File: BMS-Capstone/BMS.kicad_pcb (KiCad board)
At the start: 4 copper layers, 235 x 92.7 mm, 164 parts, among them IC1 MP2643, IC2 MP2643, IC3 MP2643, IC4 MP2643, IC5 MP2643, IC6 MP2643, IC7 BQ7694204PFBR, J1 Conn_01x02_Socket, J2 Conn_01x02_Socket, J3 Conn_01x13_Socket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

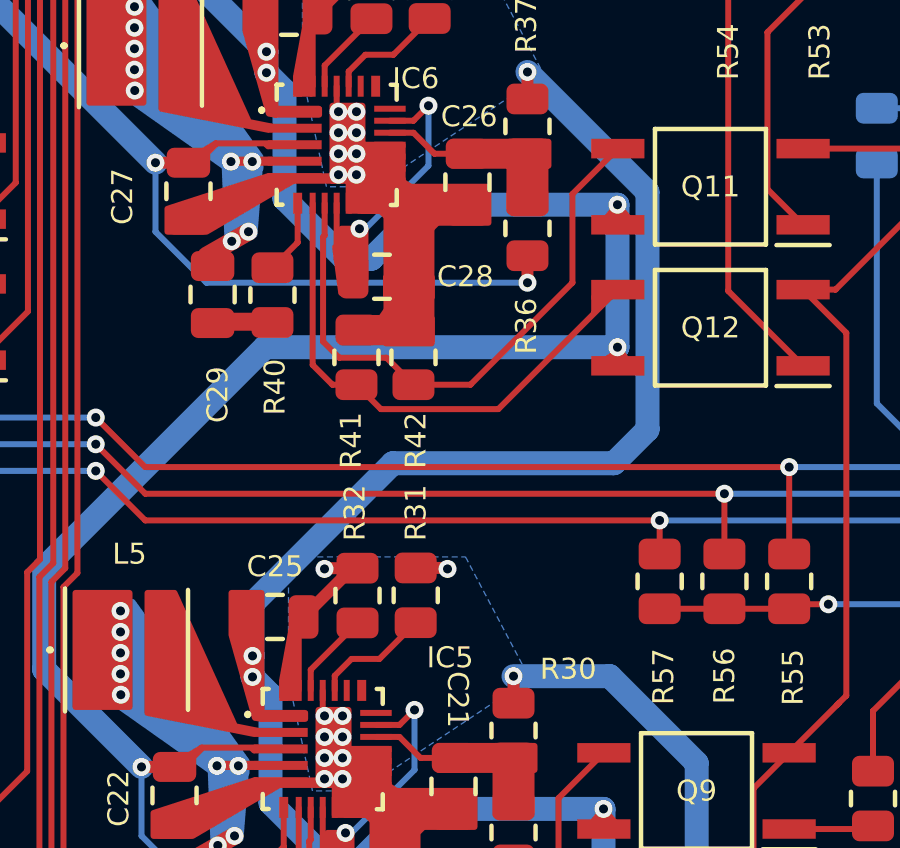
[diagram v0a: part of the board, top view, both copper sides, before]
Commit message: Added V-CUT label
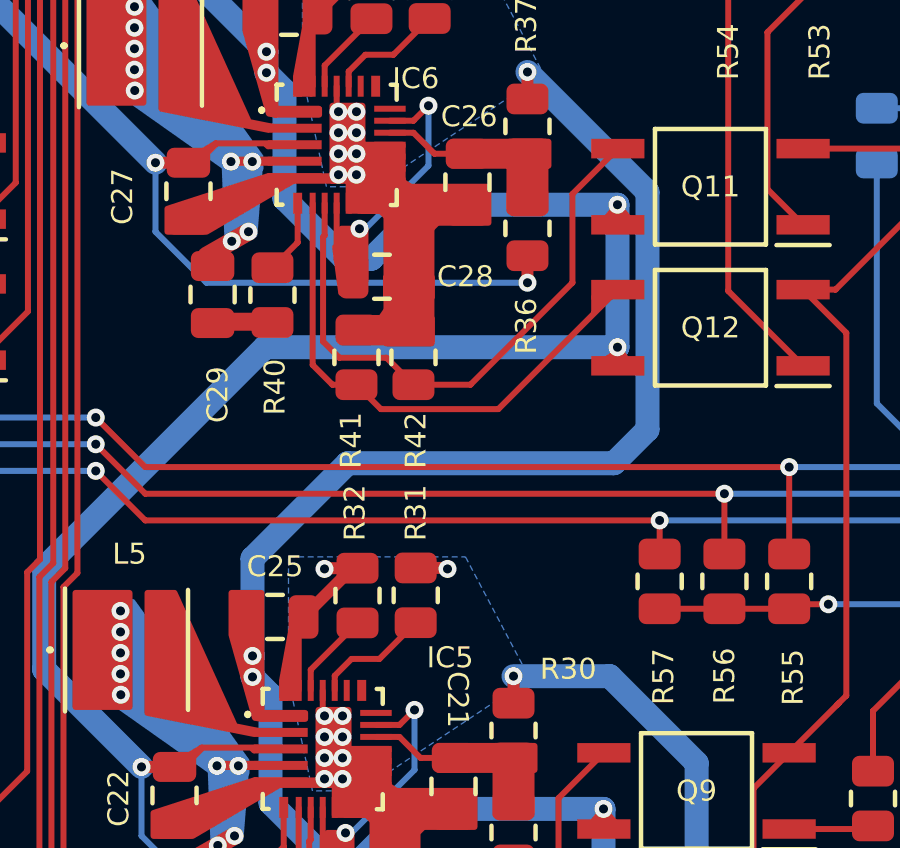
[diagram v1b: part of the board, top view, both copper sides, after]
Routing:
- net /BMS Board/4Upper: track 311.4 -> 312.2 mm
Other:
- board text added: "V-CUT"

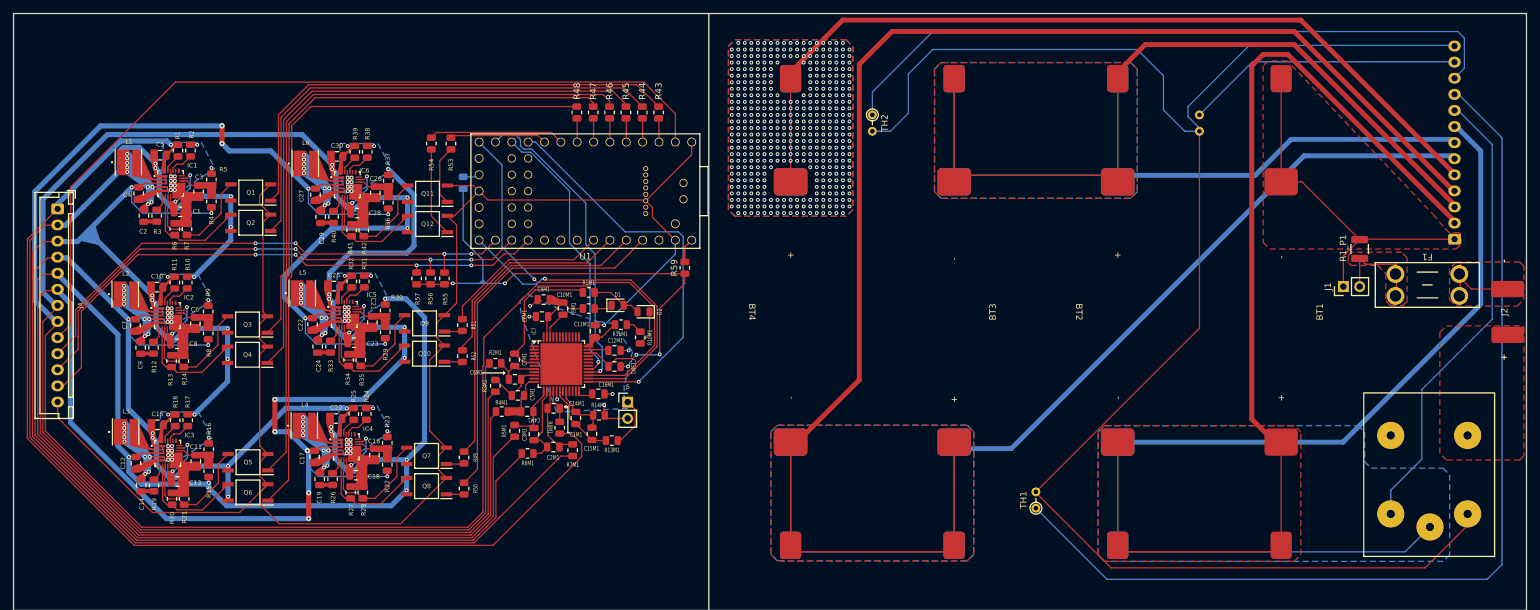
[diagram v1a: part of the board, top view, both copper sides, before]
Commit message: Added Transistors for optocouple and relay drive
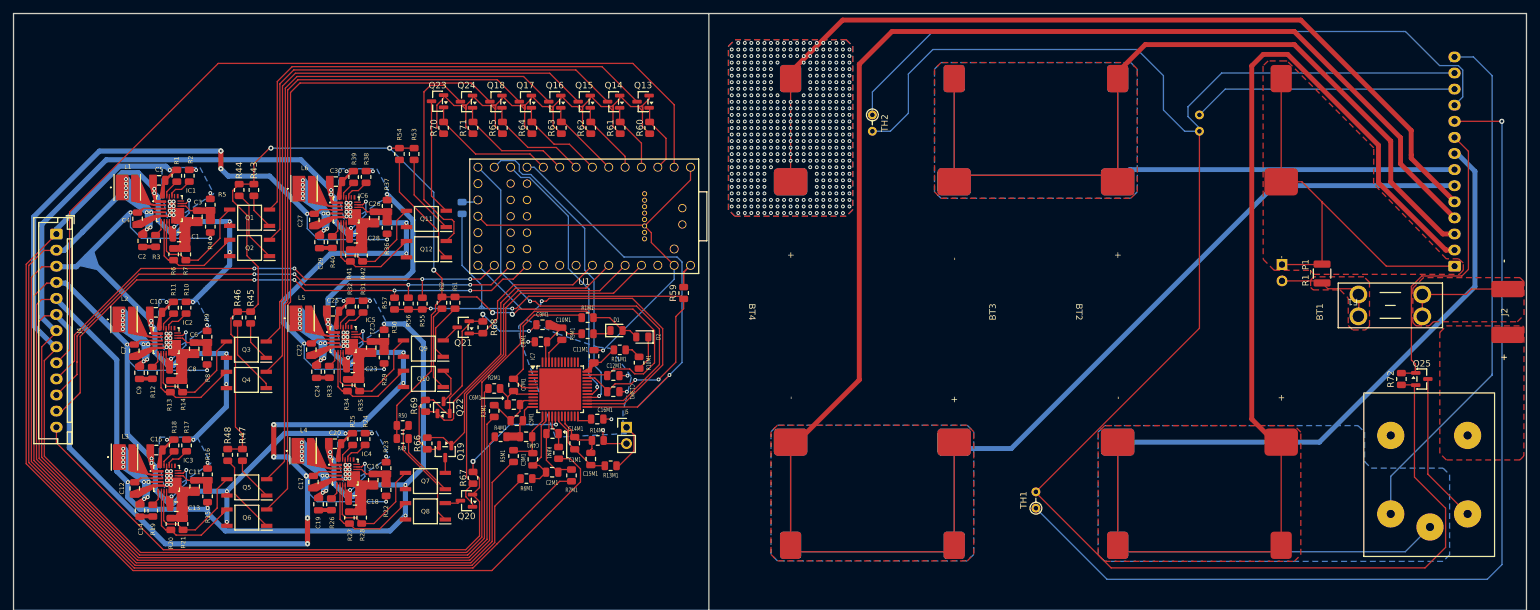
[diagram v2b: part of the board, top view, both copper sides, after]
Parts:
- added Q13: 2N7002, Package_TO_SOT_SMD:SOT-23, F.Cu at (124.3, 43.0)
- added Q14: 2N7002, Package_TO_SOT_SMD:SOT-23, F.Cu at (119.7, 43.0)
- added Q15: 2N7002, Package_TO_SOT_SMD:SOT-23, F.Cu at (115.1, 43.0)
- added Q16: 2N7002, Package_TO_SOT_SMD:SOT-23, F.Cu at (110.6, 43.0)
- added Q17: 2N7002, Package_TO_SOT_SMD:SOT-23, F.Cu at (106.0, 43.0)
- added Q18: 2N7002, Package_TO_SOT_SMD:SOT-23, F.Cu at (101.4, 43.0)
- added Q19: 2N7002, Package_TO_SOT_SMD:SOT-23, F.Cu at (93.5, 97.4)
- added Q20: 2N7002, Package_TO_SOT_SMD:SOT-23, F.Cu at (96.8, 105.0)
- added Q21: 2N7002, Package_TO_SOT_SMD:SOT-23, F.Cu at (96.3, 78.1)
- added Q22: 2N7002, Package_TO_SOT_SMD:SOT-23, F.Cu at (93.3, 90.5)
- added Q23: 2N7002, Package_TO_SOT_SMD:SOT-23, F.Cu at (92.4, 43.0)
- added Q24: 2N7002, Package_TO_SOT_SMD:SOT-23, F.Cu at (96.8, 43.0)
- added Q25: 2N7002, Package_TO_SOT_SMD:SOT-23, F.Cu at (245.2, 86.1)
- added R60: 10k, Resistor_SMD:R_0805_2012Metric, F.Cu at (125.3, 47.1)
- added R61: 10k, Resistor_SMD:R_0805_2012Metric, F.Cu at (120.7, 47.1)
- added R62: 10k, Resistor_SMD:R_0805_2012Metric, F.Cu at (116.2, 47.1)
- added R63: 10k, Resistor_SMD:R_0805_2012Metric, F.Cu at (111.6, 47.1)
- added R64: 10k, Resistor_SMD:R_0805_2012Metric, F.Cu at (107.0, 47.1)
- added R65: 10k, Resistor_SMD:R_0805_2012Metric, F.Cu at (102.4, 47.1)
- added R66: 10k, Resistor_SMD:R_0805_2012Metric, F.Cu at (90.8, 96.1)
- added R67: 10k, Resistor_SMD:R_0805_2012Metric, F.Cu at (97.9, 101.4)
- added R68: 10k, Resistor_SMD:R_0805_2012Metric, F.Cu at (99.4, 78.1)
- added R69: 10k, Resistor_SMD:R_0805_2012Metric, F.Cu at (90.5, 90.3)
- added R70: 10k, Resistor_SMD:R_0805_2012Metric, F.Cu at (93.3, 47.1)
- added R71: 10k, Resistor_SMD:R_0805_2012Metric, F.Cu at (97.9, 47.1)
- added R72: 10k, Resistor_SMD:R_0805_2012Metric, F.Cu at (242.1, 86.1)
- J1: moved to B.Cu
- J3: value Conn_01x13_Socket -> Conn_01x14_Socket; footprint Connector_JST:JST_XH_S13B-XH-A-1_1x13_P2.50mm_Horizontal -> Connector_JST:JST_XH_S14B-XH-A-1_1x14_P2.50mm_Horizontal
- R43, R44, R45, R46, R47, R48, R49, R50, R51, R52, R53, R54: value 200 -> 720
- moved R47 76.1 mm to (62.1, 97.9), turned to 90 degrees
- moved R48 76.0 mm to (59.8, 97.9), turned to 90 degrees
- moved R45 66.4 mm to (63.3, 76.6), turned to 90 degrees
- moved R46 66.0 mm to (61.3, 76.6), turned to 90 degrees
- moved R43 64.0 mm to (63.8, 56.7), turned to 90 degrees
- moved R44 63.8 mm to (61.5, 56.7), turned to 90 degrees
- moved R50 13.7 mm to (86.9, 93.3), turned to 180 degrees
- moved J1 10.1 mm to (223.5, 68.3), turned to 180 degrees
- moved R49 9.97 mm to (86.9, 95.4), turned to 180 degrees
- moved R52 8.87 mm to (93.0, 74.3)
- moved R1_P1 6.97 mm to (229.7, 69.7)
- moved F1 6.58 mm to (235.4, 73.0)
- moved R53 5.94 mm to (88.7, 51.2)
- moved R54 5.22 mm to (86.4, 51.2)
- moved R56 5.20 mm to (87.8, 74.4)
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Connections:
- C12M1 pad 1: /Monitoring/5V -> /BMS Board/5v
- IC7 pad 35: /Monitoring/5V -> /BMS Board/5v
- K1 pad 2: MCUGND -> Net-(Q25-D)
- K1 pad 6: Net-(J3-Pin_9) -> Net-(J3-Pin_14)
- Q1 pad 2: GND -> Net-(Q13-D)
- Q10 pad 2: GND -> Net-(Q22-D)
- Q11 pad 2: GND -> Net-(Q23-D)
- Q12 pad 2: GND -> Net-(Q24-D)
- Q2 pad 2: GND -> Net-(Q14-D)
- Q3 pad 2: GND -> Net-(Q15-D)
- Q4 pad 2: GND -> Net-(Q16-D)
- Q5 pad 2: GND -> Net-(Q17-D)
- Q6 pad 2: GND -> Net-(Q18-D)
- Q7 pad 2: GND -> Net-(Q19-D)
- Q8 pad 2: GND -> Net-(Q20-D)
- Q9 pad 2: GND -> Net-(Q21-D)
- R43 pad 2: /BMS Board/1MODE -> /BMS Board/5v
- R44 pad 2: /BMS Board/1EN -> /BMS Board/5v
- R45 pad 2: /BMS Board/2MODE -> /BMS Board/5v
- R46 pad 2: /BMS Board/2EN -> /BMS Board/5v
- R47 pad 2: /BMS Board/3MODE -> /BMS Board/5v
- R48 pad 2: /BMS Board/3EN -> /BMS Board/5v
- R49 pad 2: /BMS Board/4MODE -> /BMS Board/5v
- R50 pad 2: /BMS Board/4EN -> /BMS Board/5v
- R51 pad 2: /BMS Board/5MODE -> /BMS Board/5v
- R52 pad 2: /BMS Board/5EN -> /BMS Board/5v
- R53 pad 2: /BMS Board/6MODE -> /BMS Board/5v
- R54 pad 2: /BMS Board/6EN -> /BMS Board/5v
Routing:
- net /BMS Board/5v: track 0.00 -> 184.5 mm, vias 0 -> 5
- net Net-(Q17-D): track 0.00 -> 99.8 mm
- net Net-(Q18-D): track 0.00 -> 99.1 mm
- net Net-(Q5-Pad1): track 105.0 -> 6.96 mm
- net Net-(Q6-Pad1): track 105.5 -> 12.6 mm
- net Net-(Q15-D): track 0.00 -> 89.3 mm
- net Net-(Q16-D): track 0.00 -> 88.6 mm
- net Net-(Q3-Pad1): track 90.3 -> 6.36 mm
- net Net-(J3-Pin_14): track 0.00 -> 82.7 mm
- net Net-(Q4-Pad1): track 91.9 -> 11.9 mm
- net Net-(Q13-D): track 0.00 -> 79.5 mm
- net Net-(Q14-D): track 0.00 -> 78.7 mm
- net Net-(Q1-Pad1): track 76.2 -> 5.67 mm
- net Net-(Q2-Pad1): track 77.5 -> 11.4 mm
- net GND: track 267.9 -> 309.2 mm, vias 8 -> 10
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- added copper zone on F.Cu, net GND

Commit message: Fixed up edge cuts and other DRC
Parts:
- moved C12 6.20 mm to (44.1, 97.0)
- moved C16 6.20 mm to (81.2, 95.7)
- moved C17 6.20 mm to (71.9, 96.0)
- moved C19 6.20 mm to (72.7, 99.5)
- moved C1M1 6.20 mm to (109.0, 88.5)
- moved C20 6.20 mm to (75.2, 90.1)
- moved C21 6.20 mm to (80.8, 75.2)
- moved C22 6.20 mm to (71.5, 75.5)
- moved C25 6.20 mm to (74.9, 69.5)
- moved C4 6.20 mm to (44.5, 55.1)
- moved C6M1 6.20 mm to (103.0, 84.0)
- moved C7 6.20 mm to (44.0, 75.6)
- moved IC4 6.20 mm to (76.8, 94.5)
- moved IC5 6.20 mm to (76.5, 73.9)
- moved L5 6.20 mm to (69.9, 70.6)
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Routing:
- net GND: track 309.2 -> 310.7 mm, vias 10 -> 11
- net /BMS Board/1GND: track 174.1 -> 174.8 mm
- net /BMS Board/5v: track 184.5 -> 185.1 mm
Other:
- board size 235 x 92.7 mm -> 244 x 92.5 mm

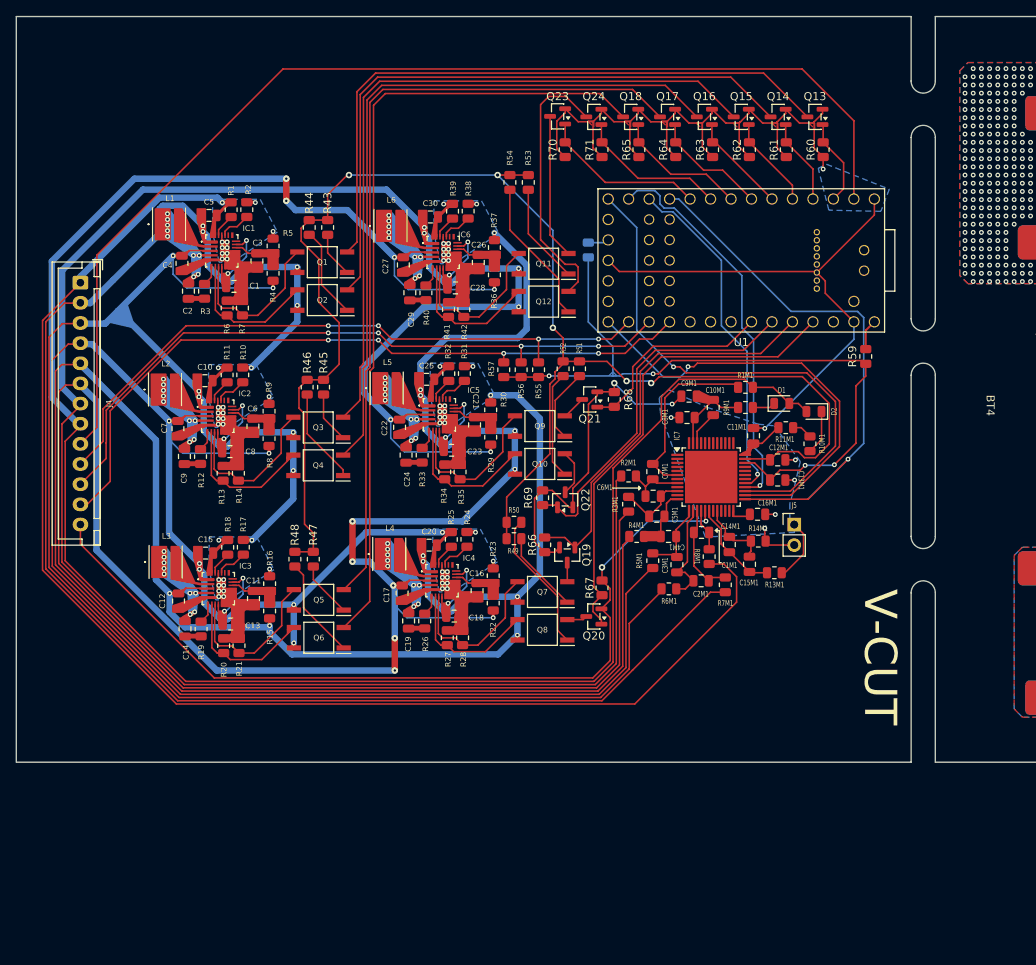
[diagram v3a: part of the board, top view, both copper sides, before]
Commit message: Changed v cut and some small corrections
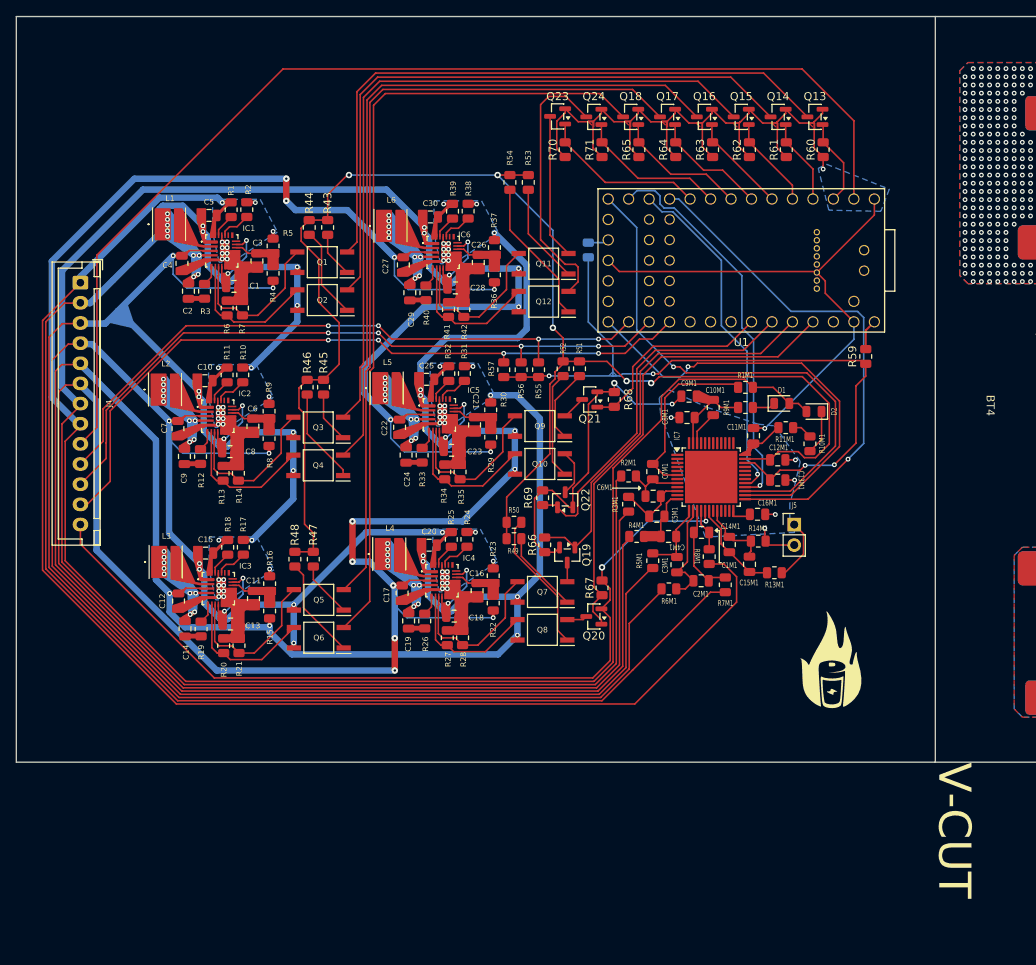
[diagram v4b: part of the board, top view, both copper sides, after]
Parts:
- added G***: LOGO, LOGO, F.Cu at (125.0, 104.2)
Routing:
- net /Monitoring/INT: track 70.3 -> 63.4 mm
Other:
- outline, holes or cut-outs redrawn

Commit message: cool logo :)
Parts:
- moved G*** 1.77 mm to (123.2, 104.0)
